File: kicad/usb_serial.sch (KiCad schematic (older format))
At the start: 19 parts, among them J13 USB_C_Receptacle_USB2.0, Q3 BC817DS,115, U5 CP2102N-A01-GQFN28

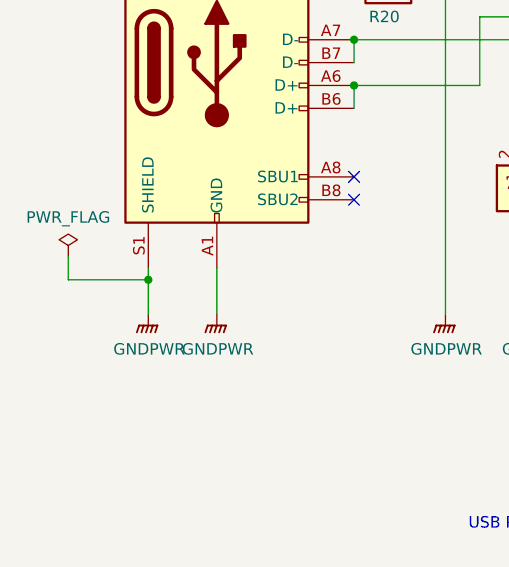
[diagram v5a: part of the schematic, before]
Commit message: Relabeled and completed ERC
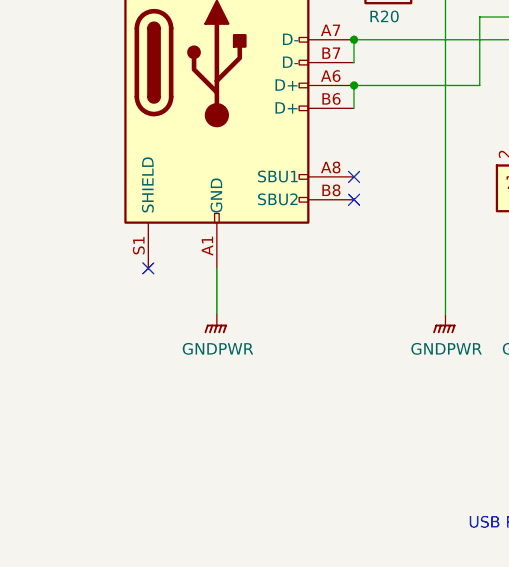
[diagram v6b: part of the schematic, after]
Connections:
- net GNDPWR: no longer J13.S1 (SHIELD)
- no-connect marks 15 -> 16
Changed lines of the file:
@@
 	5400 2200 5400 2450
 $Comp
-L power:GNDPWR #PWR065
+L power:GNDPWR #PWR064
 U 1 1 610C1F08
 P 2450 4450
-F 0 "#PWR065" H 2450 4250 50  0001 C CNN
+F 0 "#PWR064" H 2450 4250 50  0001 C CNN
 F 1 "GNDPWR" H 2454 4296 50  0000 C CNN
 F 2 "" H 2450 4400 50  0001 C CNN
@@
 $EndComp
 $Comp
-L power:GNDPWR #PWR066
+L power:GNDPWR #PWR065
 U 1 1 610D2CDA
 P 3450 4450
-F 0 "#PWR066" H 3450 4250 50  0001 C CNN
+F 0 "#PWR065" H 3450 4250 50  0001 C CNN
 F 1 "GNDPWR" H 3454 4296 50  0000 C CNN
 F 2 "" H 3450 4400 50  0001 C CNN
@@
 	3050 3450 3600 3450
 $Comp
-L power:GNDPWR #PWR068
+L power:GNDPWR #PWR067
 U 1 1 610EA7EC
 P 5400 5050
-F 0 "#PWR068" H 5400 4850 50  0001 C CNN
+F 0 "#PWR067" H 5400 4850 50  0001 C CNN
 F 1 "GNDPWR" H 5404 4896 50  0000 C CNN
 F 2 "" H 5400 5000 50  0001 C CNN
@@
 USB Port and CP2102N
 $Comp
-L power:GNDPWR #PWR067
+L power:GNDPWR #PWR066
 U 1 1 61157A36
 P 3850 4450
-F 0 "#PWR067" H 3850 4250 50  0001 C CNN
+F 0 "#PWR066" H 3850 4250 50  0001 C CNN
 F 1 "GNDPWR" H 3854 4296 50  0000 C CNN
 F 2 "" H 3850 4400 50  0001 C CNN
@@
 	1    0    0    -1
 $EndComp
-$Comp
-L power:GNDPWR #PWR064
-U 1 1 61797B7A
-P 2150 4450
-F 0 "#PWR064" H 2150 4250 50  0001 C CNN
-F 1 "GNDPWR" H 2154 4296 50  0000 C CNN
-F 2 "" H 2150 4400 50  0001 C CNN
-F 3 "" H 2150 4400 50  0001 C CNN
-	1    2150 4450
-	1    0    0    -1
-$EndComp
-Wire Wire Line
-	2150 4250 2150 4300
 Wire Wire Line
 	6150 1700 6150 1850
@@
 Wire Wire Line
 	5800 1850 5800 1700
-$Comp
-L power:PWR_FLAG #FLG05
-U 1 1 617BC8F0
-P 1800 4200
-F 0 "#FLG05" H 1800 4275 50  0001 C CNN
-F 1 "PWR_FLAG" H 1800 4373 50  0000 C CNN
-F 2 "" H 1800 4200 50  0001 C CNN
-F 3 "~" H 1800 4200 50  0001 C CNN
-	1    1800 4200
-	1    0    0    -1
-$EndComp
-Wire Wire Line
-	1800 4200 1800 4300
-Wire Wire Line
-	1800 4300 2150 4300
-Connection ~ 2150 4300
-Wire Wire Line
-	2150 4300 2150 4450
 Text HLabel 5900 3850 2    50   Output ~ 0
 CH_CHREN
@@
 NoConn ~ 5900 4850
 NoConn ~ 5900 3550
+NoConn ~ 2150 4250
 $EndSCHEMATC
